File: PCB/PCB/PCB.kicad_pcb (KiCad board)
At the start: 2 copper layers, 3 parts

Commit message: PCB getekend
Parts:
- removed REF** (x2): PinHeader_1x01_P1.00mm_Vertical, Connector_PinHeader_1.00mm:PinHeader_1x01_P1.00mm_Vertical
- removed REF**: USB_C_Receptacle_HCTL_HC-TYPE-C-16P-01A, Connector_USB:USB_C_Receptacle_HCTL_HC-TYPE-C-16P-01A
- added LED: Conn_01x03_Socket, Connector_PinSocket_2.54mm:PinSocket_1x03_P2.54mm_Vertical, F.Cu at (98.4, 96.0)
- added Sensor: Conn_01x03_Socket, Connector_PinSocket_2.54mm:PinSocket_1x03_P2.54mm_Vertical, F.Cu at (106.6, 105.0)
- added U1: ESP32-C3-DEVKITM-1, ESP32-C3-DEVKITM-1:XCVR_ESP32-C3-DEVKITM-1, F.Cu at (82.3, 106.2)
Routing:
- net 5V: track 0.00 -> 21.6 mm
- net Sensor: track 0.00 -> 13.6 mm
- net LED: track 0.00 -> 6.66 mm
- added copper zone on B.Cu, net GND
- added copper zone on F.Cu, net GND
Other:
- board outline added: 42.4 x 43.5 mm
- board text added: "5V"
- board text added: "GND"
- board text added: "LED"
- board text added: "Sensor"

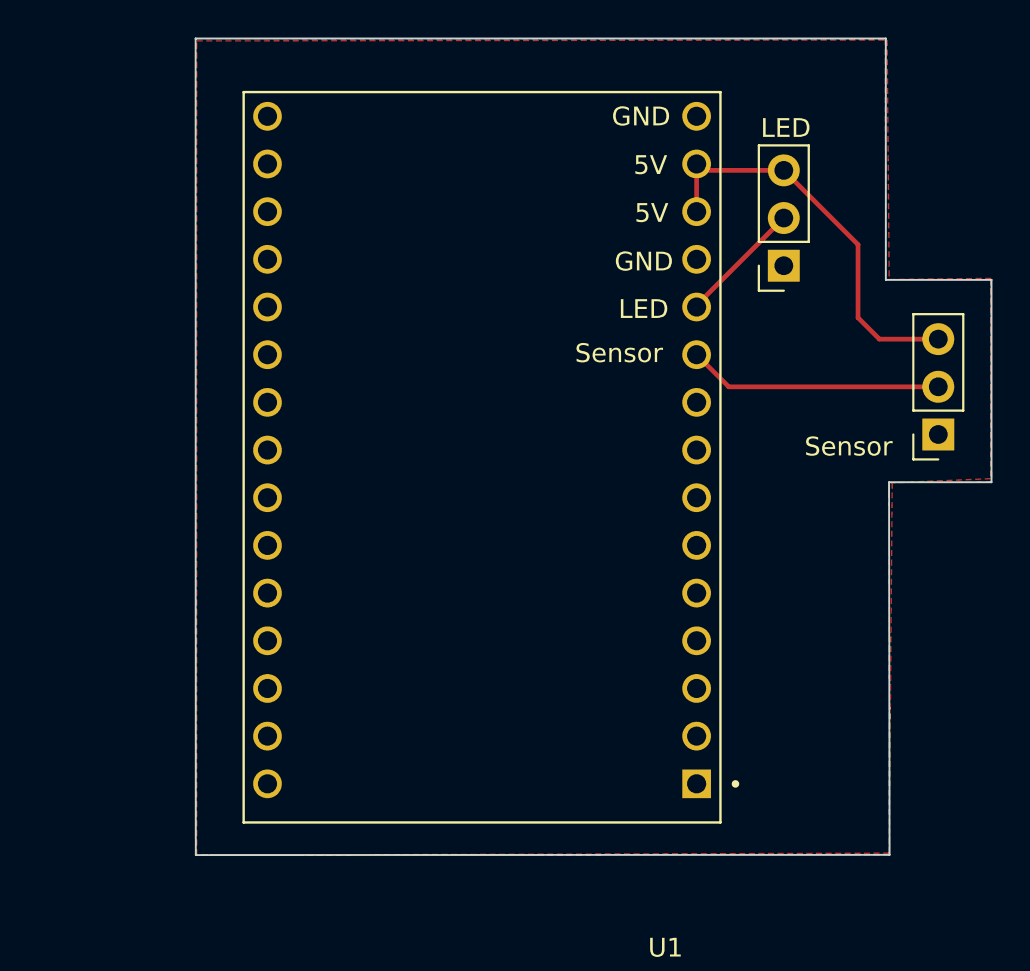
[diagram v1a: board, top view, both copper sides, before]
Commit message: deleted unused pcb files
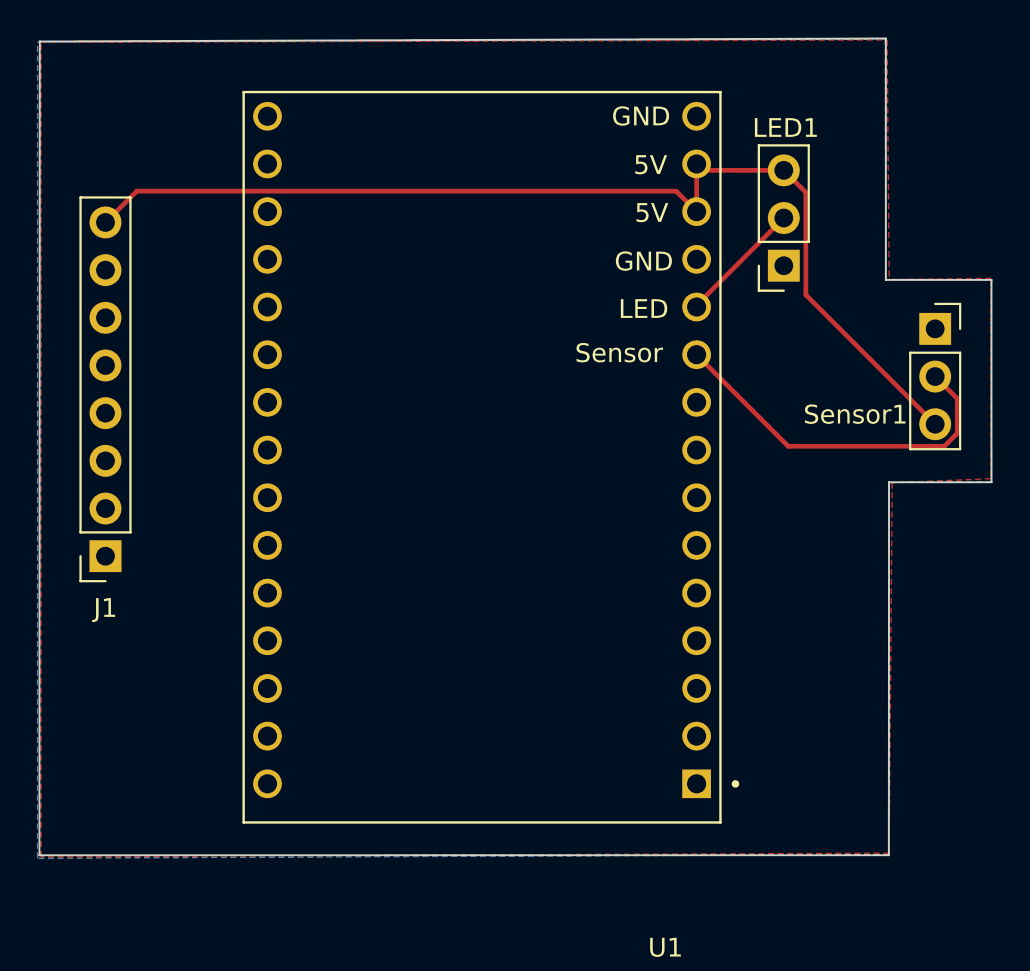
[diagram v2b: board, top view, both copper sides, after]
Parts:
- added J1: Conn_01x08_Socket, Connector_PinSocket_2.54mm:PinSocket_1x08_P2.54mm_Vertical, F.Cu at (62.3, 111.5)
- moved Sensor1 5.63 mm to (106.5, 99.4), turned to 0 degrees
- renumbered LED to LED1, Sensor to Sensor1
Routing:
- net 5V: track 21.6 -> 56.8 mm
- net Sensor: track 13.6 -> 19.7 mm
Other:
- board size 42.4 x 43.5 mm -> 50.7 x 43.5 mm

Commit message: Readme bijgevuld en schema gemaakt
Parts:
- J1: value Conn_01x08_Socket -> USB-C
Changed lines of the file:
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@@
         (effects (font (size 1 1) (thickness 0.15)))
     )
-    (fp_text value "Conn_01x08_Socket" (at 0 20.55) (layer "F.Fab")
+    (fp_text value "USB-C" (at 0 20.55) (layer "F.Fab")
         (effects (font (size 1 1) (thickness 0.15)))
     )
